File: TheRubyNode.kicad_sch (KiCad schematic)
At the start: 61 parts, among them J1 USB4085-GF-A_REVB, J2 Conn_02x01, J3 Conn_02x01, J4 Conn_01x02, J5 91930-21111LF, J6 Conn_01x04, J7 Conn_01x03, Q1 Si2307, SW1 SW_SPST, SW2 SW_Push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

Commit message: Finish footprints, start of pcb
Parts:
- added H1, H2, H3, H4: MountingHole_Pad, MountingHole:MountingHole_3.2mm_M3_Pad, symbol Mechanical:MountingHole_Pad
- J2, J3, J4, SW2: footprint Connector_JST:JST_PH_B2B-PH-K_1x02_P2.00mm_Vertical -> Connector_JST:JST_PH_S2B-PH-SM4-TB_1x02-1MP_P2.00mm_Horizontal
- R3: value 2m -> 0.1R; footprint Resistor_THT:R_Axial_DIN0516_L15.5mm_D5.0mm_P20.32mm_Horizontal -> Resistor_SMD:R_2512_6332Metric_Pad1.40x3.35mm_HandSolder
- SW1: footprint Connector_JST:JST_PH_B2B-PH-K_1x02_P2.00mm_Vertical -> Connector_JST:JST_PH_B2B-PH-SM4-TB_1x02-1MP_P2.00mm_Vertical
- SW3, SW4: footprint Button_Switch_THT:SW_PUSH_6mm_H4.3mm -> Button_Switch_SMD:SW_SPST_PTS645
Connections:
- no-connect marks 19 -> 23

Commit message: Add PCB design
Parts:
- added J8: Conn_02x01, Connector_JST:JST_PH_B2B-PH-SM4-TB_1x02-1MP_P2.00mm_Vertical, symbol Connector_Generic:Conn_02x01
- SW2: footprint Connector_JST:JST_PH_S2B-PH-SM4-TB_1x02-1MP_P2.00mm_Horizontal -> Connector_JST:JST_PH_B2B-PH-SM4-TB_1x02-1MP_P2.00mm_Vertical
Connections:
- net +3V3: now also U5.2 (3V3)
- net +5V: now also J8.1 (Pin_1)
- net GND: now also C10.2, C9.2, J2.1 (Pin_1), J3.1 (Pin_1), R2.2, R7.1, J8.2 (Pin_2); no longer J2.2 (Pin_2), J3.2 (Pin_2), R2.1, R7.2
- net I2C_SCL: now also U5.11 (IO18); no longer U5.10 (IO17)
- net I2C_SDA: now also U5.10 (IO17); no longer U5.11 (IO18)
- net LR_BUSY: now also U5.19 (IO11); no longer U5.17 (IO9)
- net LR_IRQ: now also U5.17 (IO9); no longer U5.19 (IO11)
- net at C1.1, Q1.3 (D), U1.8 (IN+): now also R3.1; no longer R3.2
- net at C1.2, U1.7 (IN-): now also R3.2, SW1.1 (A); no longer R3.1, SW1.2 (B)
- net at U4.6 (PROG): now also R7.2; no longer R7.1
- net IO45: now reaches U5.26 (IO45)
- net IO45: now also J5.1
- net at J1.B5 (CC2): now also R2.1; no longer R2.2
- net IO1: no longer names the net of U5.39 (IO1)
- net IO1: no longer J5.1
- new net: BT1.1 (+), J2.2 (Pin_2), J3.2 (Pin_2), SW1.2 (B)
- no-connect marks 23 -> 22
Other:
- moved on the sheet: C10, C9, J2, J3, R10, R2, R3, SW1

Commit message: Finalise rev 1.0 of PCB
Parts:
- J6: footprint Connector_JST:JST_SH_SM04B-SRSS-TB_1x04-1MP_P1.00mm_Horizontal -> Connector_JST:JST_SH_BM04B-SRSS-TB_1x04-1MP_P1.00mm_Vertical
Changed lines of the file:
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@@
 			)
 		)
-		(property "Footprint" "Connector_JST:JST_SH_SM04B-SRSS-TB_1x04-1MP_P1.00mm_Horizontal"
+		(property "Footprint" "Connector_JST:JST_SH_BM04B-SRSS-TB_1x04-1MP_P1.00mm_Vertical"
 			(at 254 157.48 0)
 			(effects

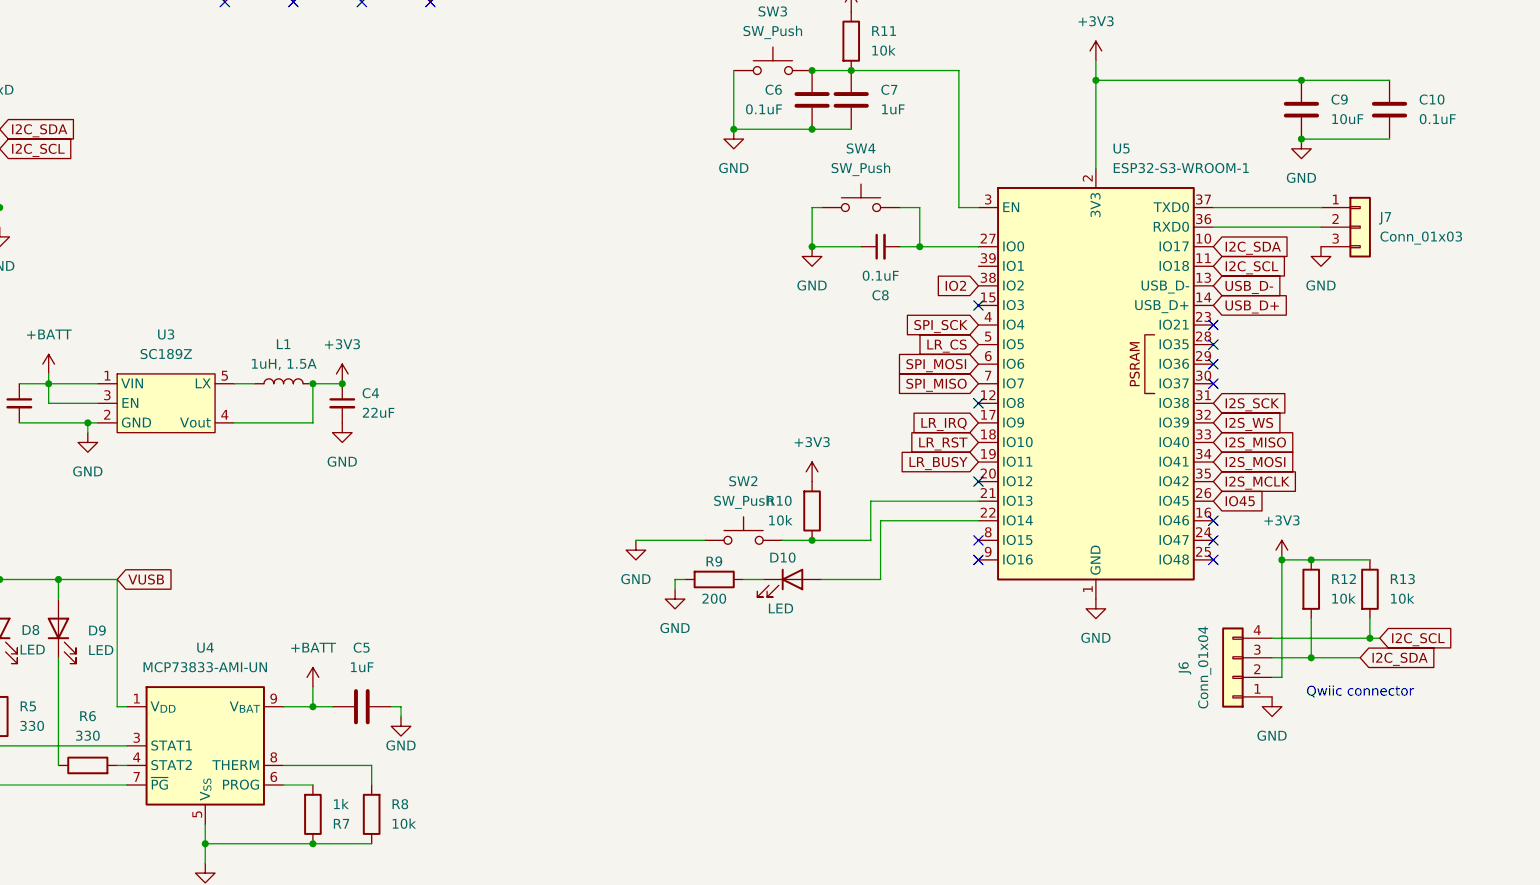
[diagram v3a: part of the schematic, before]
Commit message: Break out additional IOs
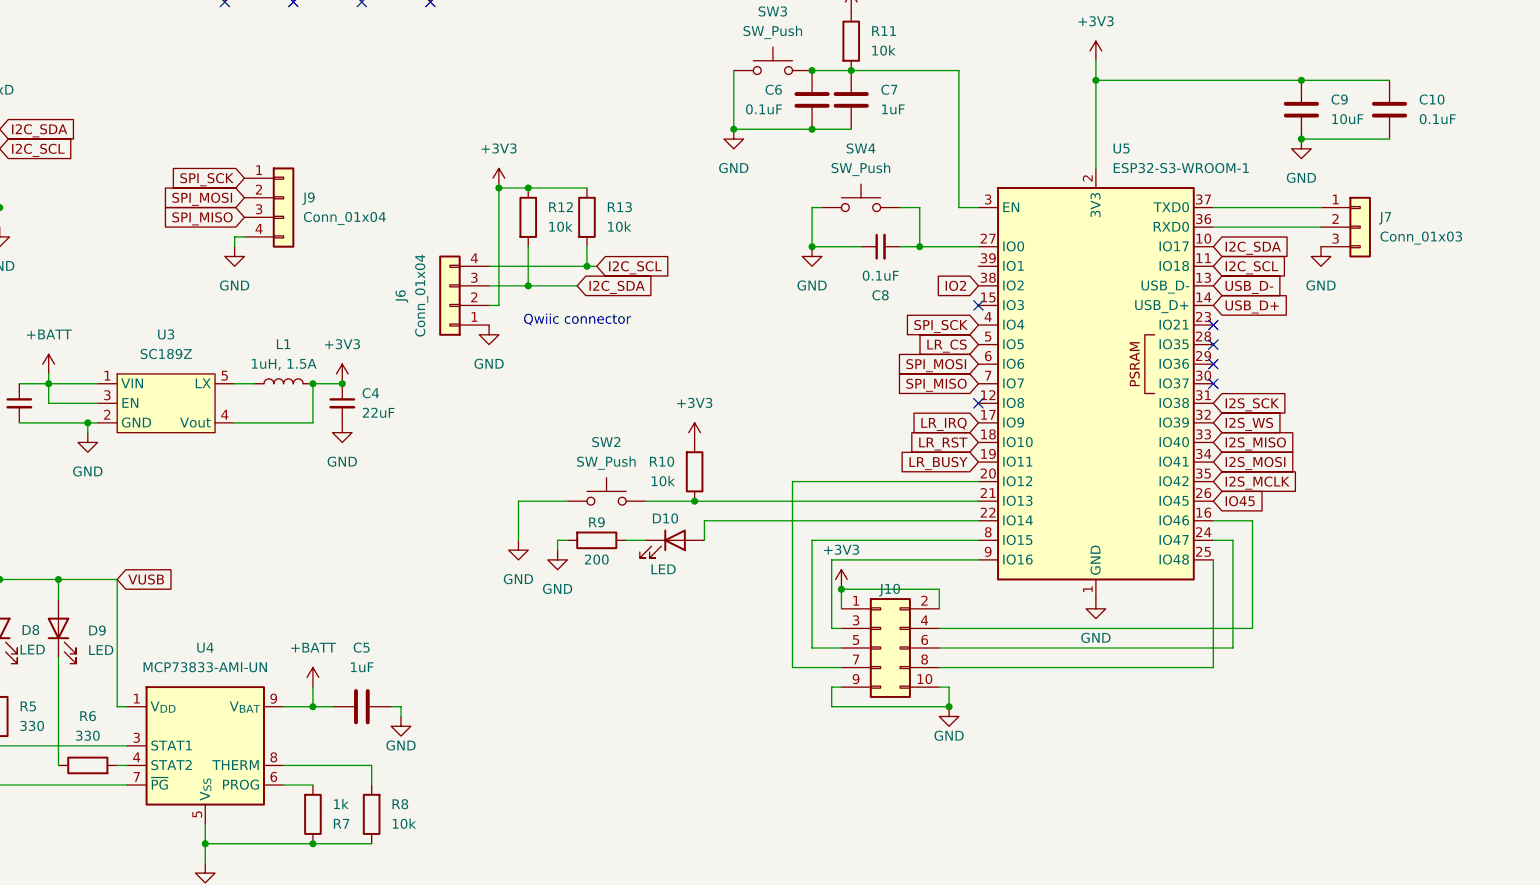
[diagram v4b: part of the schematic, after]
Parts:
- added J10: Conn_02x05_Odd_Even, Connector_PinSocket_2.54mm:PinSocket_2x05_P2.54mm_Vertical, symbol Connector_Generic:Conn_02x05_Odd_Even
- added J9: Conn_01x04, Connector_PinHeader_2.54mm:PinHeader_1x04_P2.54mm_Vertical, symbol Connector_Generic:Conn_01x04
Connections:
- net +3V3: now also J10.1 (Pin_1), J10.2 (Pin_2)
- net GND: now also J10.10 (Pin_10), J10.9 (Pin_9), J9.4 (Pin_4)
- net SPI_MISO: now also J9.3 (Pin_3)
- net SPI_MOSI: now also J9.2 (Pin_2)
- net SPI_SCK: now also J9.1 (Pin_1)
- net at U5.16 (IO46): now also J10.4 (Pin_4)
- net at U5.20 (IO12): now also J10.7 (Pin_7)
- net at U5.24 (IO47): now also J10.6 (Pin_6)
- net at U5.25 (IO48): now also J10.8 (Pin_8)
- net at U5.8 (IO15): now also J10.5 (Pin_5)
- net at U5.9 (IO16): now also J10.3 (Pin_3)
- no-connect marks 22 -> 16
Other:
- moved on the sheet: D10, J6, R10, R12, R13, R9, SW2

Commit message: Add pin labels
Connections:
- net IO46: now reaches J10.4 (Pin_4), U5.16 (IO46)
- net IO12: now reaches J10.7 (Pin_7), U5.20 (IO12)
- net IO47: now reaches J10.6 (Pin_6), U5.24 (IO47)
- net IO48: now reaches J10.8 (Pin_8), U5.25 (IO48)
- net IO15: now reaches J10.5 (Pin_5), U5.8 (IO15)
- net IO16: now reaches J10.3 (Pin_3), U5.9 (IO16)
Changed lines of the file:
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@@
+		)
+	)
+	(label "IO16"
+		(at 209.55 142.24 0)
+		(effects
+			(font
+				(size 1.27 1.27)
+			)
+			(justify left bottom)
+		)
+	)
+	(label "IO48"
+		(at 251.46 142.24 0)
+		(effects
+			(font
+				(size 1.27 1.27)
+			)
+			(justify left bottom)
+		)
+	)
+	(label "IO47"
+		(at 254 139.7 0)
+		(effects
+			(font
+				(size 1.27 1.27)
+			)
+			(justify left bottom)
+		)
+	)
+	(label "IO15"
+		(at 209.55 139.7 0)
+		(effects
+			(font
+				(size 1.27 1.27)
+			)
+			(justify left bottom)
+		)
+	)
+	(label "IO46"
+		(at 256.54 137.16 0)
+		(effects
+			(font
+				(size 1.27 1.27)
+			)
+			(justify left bottom)
+		)
+	)
+	(label "IO12"
+		(at 200.66 132.08 0)
+		(effects
+			(font
+				(size 1.27 1.27)
+			)
+			(justify left bottom)
 		)
 	)
